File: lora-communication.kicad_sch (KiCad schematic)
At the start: 33 parts, among them J4 Conn_Coaxial, U401 SX1262, U402 PE4259, Y3 Crystal_GND24

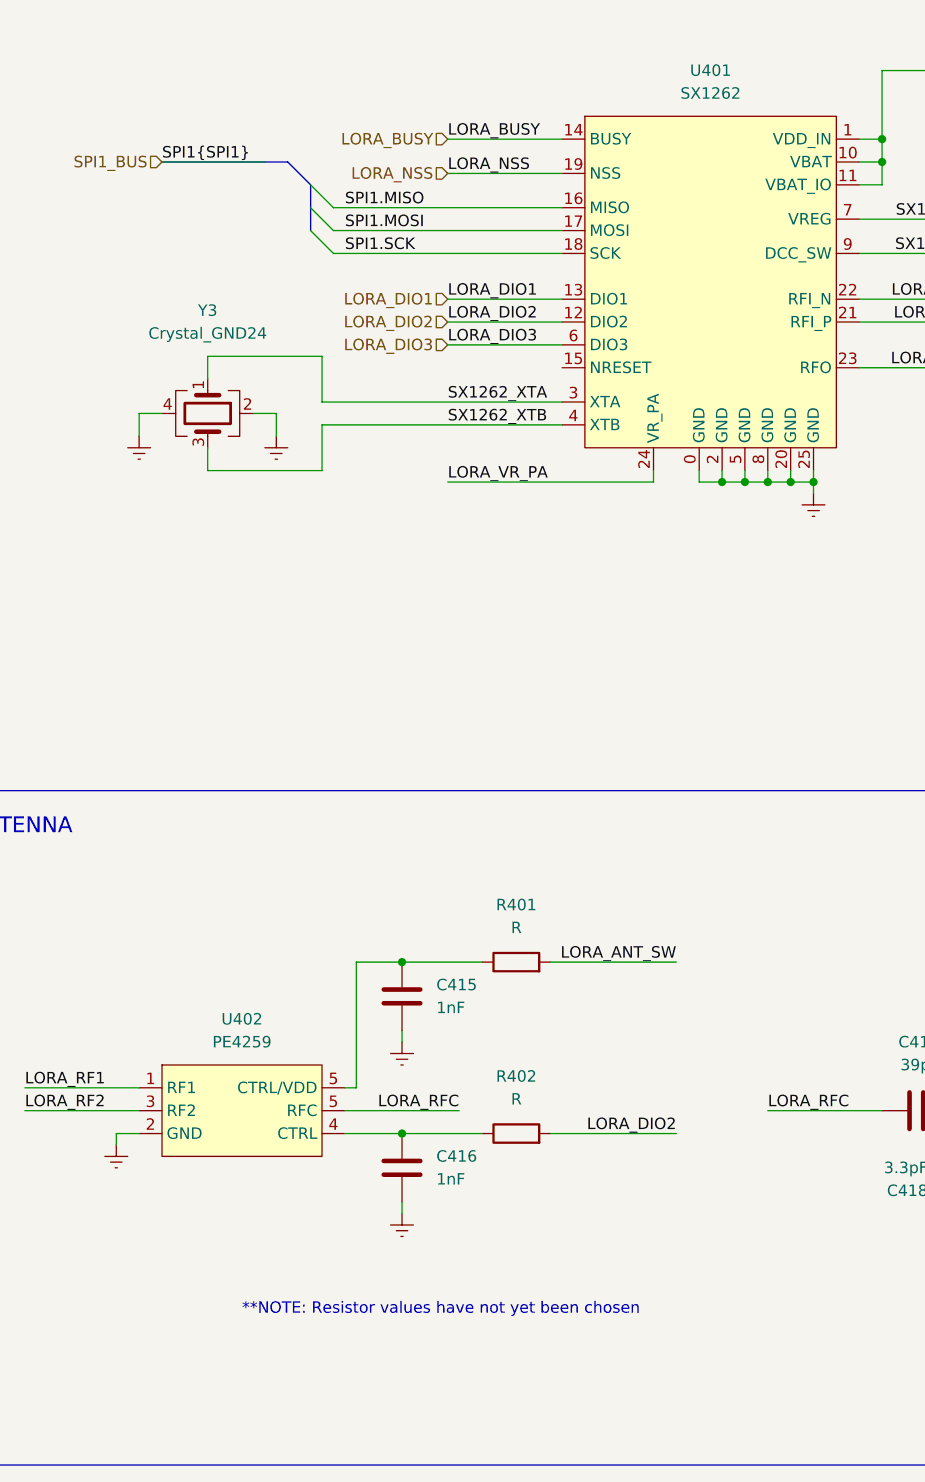
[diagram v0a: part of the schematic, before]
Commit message: updated bus aliases; added resistor values to RF section; added component to Fruitly_RF library
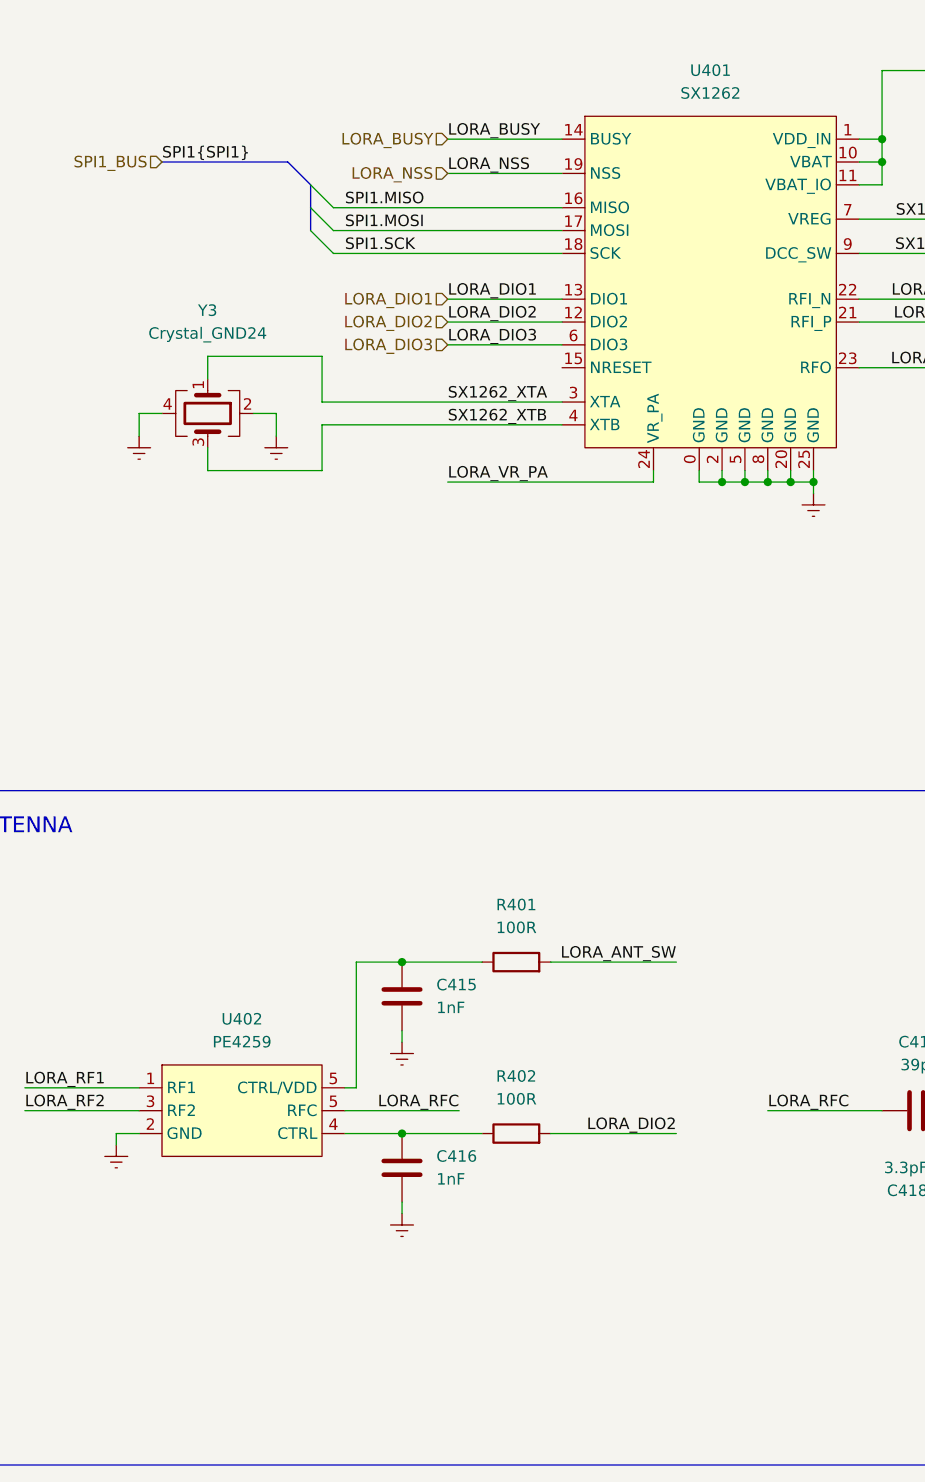
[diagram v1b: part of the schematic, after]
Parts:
- R401, R402: value R -> 100R
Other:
- note removed: "**NOTE: Resistor values have not yet been chosen"
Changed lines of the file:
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@@
     (company "Cerebral Systems Inc.")
   )
+  (bus_alias "SPI1" (members "MISO" "MOSI" "SCK"))
   (junction (at 110.49 87.63) (diameter 0) (color 0 0 0 0)
   )
@@
   )
   (wire (pts (xy 22.86 157.48) (xy 35.56 157.48))
-    (stroke (width 0) (type default) (color 0 0 0 0))
-  )
-  (wire (pts (xy 38.1 52.07) (xy 49.53 52.07))
     (stroke (width 0) (type default) (color 0 0 0 0))
   )
@@
   (text "ANTENNA IMPEDANCE MATCHING CIRCUIT" (at 177.8 81.28 0)
     (effects (font (size 1.75 1.75)) (justify left bottom))
-  )
-  (text "**NOTE: Resistor values have not yet been chosen" (at 46.99 180.34 0)
-    (effects (font (size 1.27 1.27)) (justify left bottom))
   )
   (label "SPI1.MISO" (at 58.42 57.15 0)
@@
     (in_bom yes) (on_board yes)
     (property "Reference" "R401" (id 0) (at 77.47 134.62 90))
-    (property "Value" "R" (id 1) (at 77.47 137.16 90))
+    (property "Value" "100R" (id 1) (at 77.47 137.16 90))
     (property "Footprint" "Resistor_SMD:R_0402_1005Metric" (id 2) (at 77.47 142.748 90)
       (effects (font (size 1.27 1.27)) hide)
@@
     (in_bom yes) (on_board yes)
     (property "Reference" "R402" (id 0) (at 77.47 153.67 90))
-    (property "Value" "R" (id 1) (at 77.47 156.21 90))
+    (property "Value" "100R" (id 1) (at 77.47 156.21 90))
     (property "Footprint" "Resistor_SMD:R_0402_1005Metric" (id 2) (at 77.47 161.798 90)
       (effects (font (size 1.27 1.27)) hide)

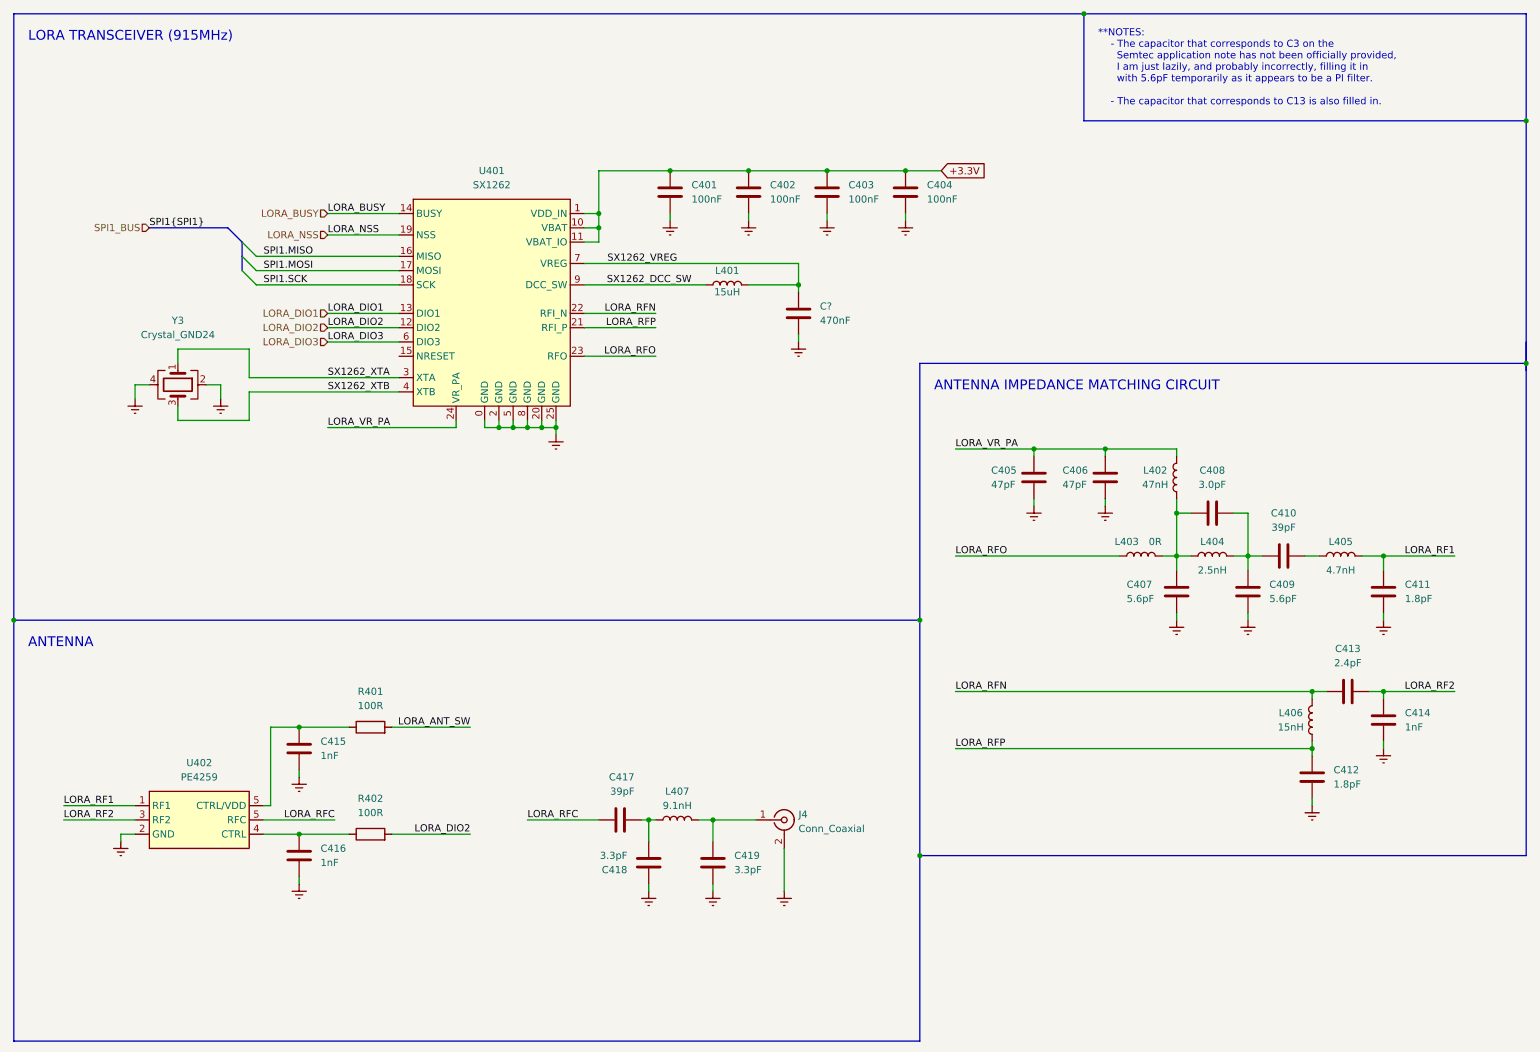
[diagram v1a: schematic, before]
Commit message: changed impedance matching circuit to IPD (integrated impedance device); updated RF switch
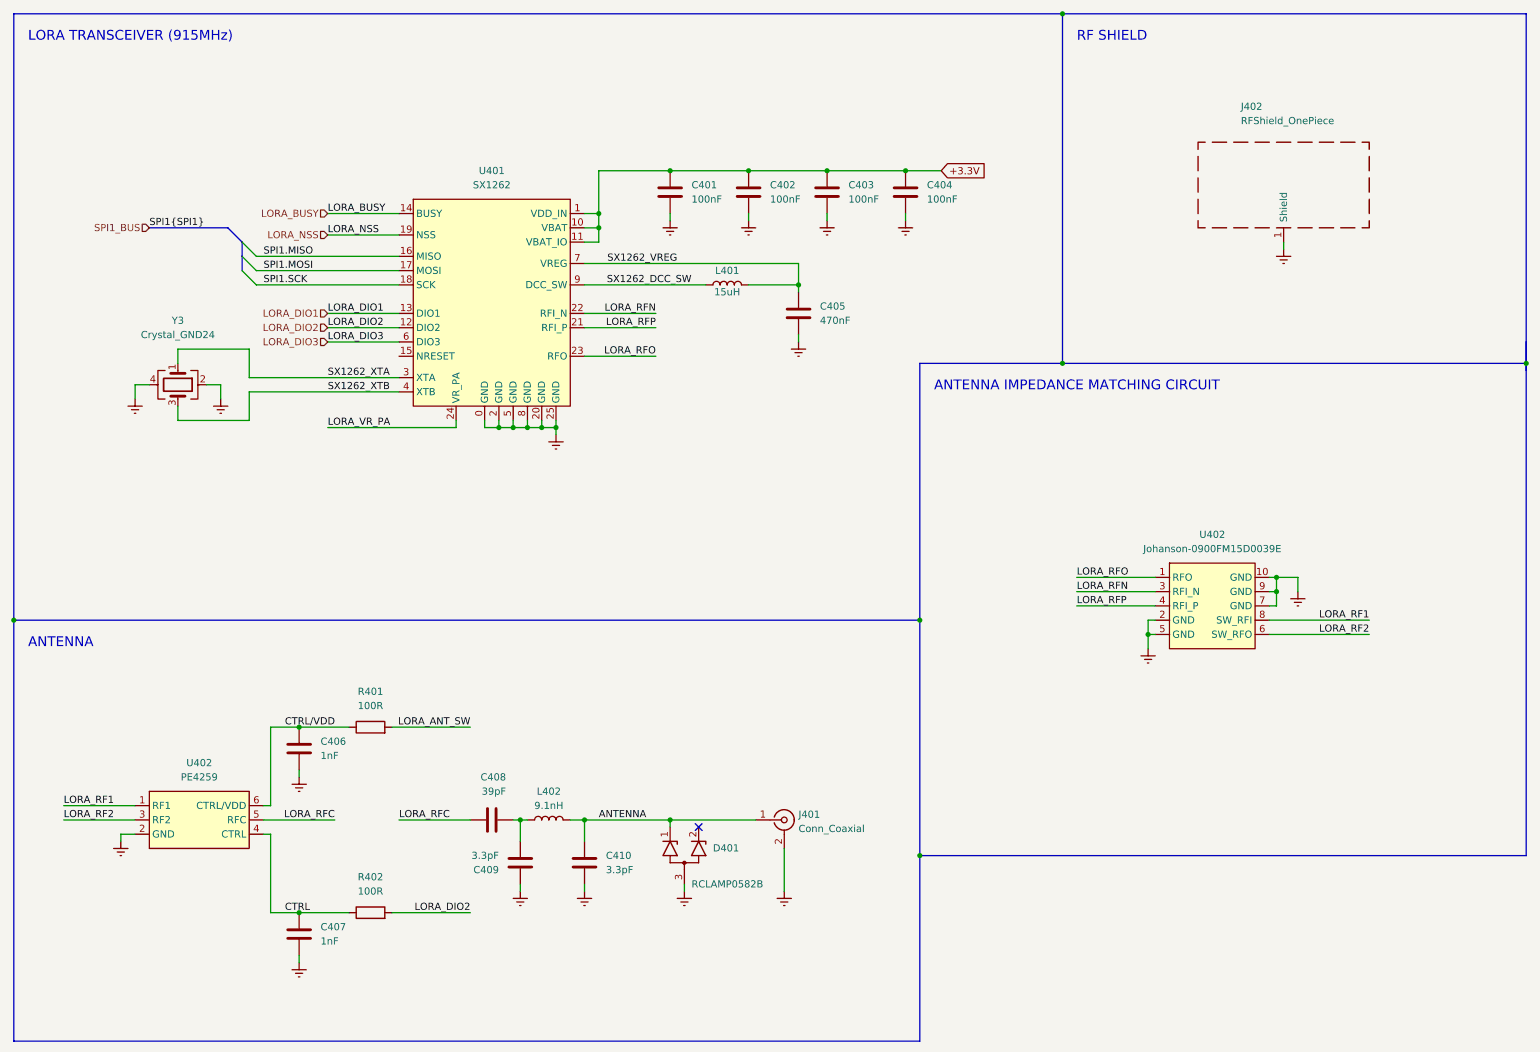
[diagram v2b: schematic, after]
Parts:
- removed C405, C406: 47pF, Capacitor_SMD:C_0402_1005Metric, symbol Device:C
- removed C407, C409: 5.6pF, Capacitor_SMD:C_0402_1005Metric, symbol Device:C
- removed C408: 3.0pF, Capacitor_SMD:C_0402_1005Metric, symbol Device:C
- removed C410: 39pF, Capacitor_SMD:C_0402_1005Metric, symbol Device:C
- removed C411, C412: 1.8pF, Capacitor_SMD:C_0402_1005Metric, symbol Device:C
- removed C413: 2.4pF, Capacitor_SMD:C_0402_1005Metric, symbol Device:C
- removed C414: 1nF, Capacitor_SMD:C_0402_1005Metric, symbol Device:C
- removed L402: 47nH, Inductor_SMD:L_0402_1005Metric, symbol Device:L
- removed L403: 0R, Inductor_SMD:L_0402_1005Metric, symbol Device:L
- removed L404: 2.5nH, Inductor_SMD:L_0402_1005Metric, symbol Device:L
- removed L405: 4.7nH, Inductor_SMD:L_0402_1005Metric, symbol Device:L
- removed L406: 15nH, Inductor_SMD:L_0402_1005Metric, symbol Device:L
- removed U402: PE4259, symbol Fruitfly_RF:PE4259
- added D401: RCLAMP0582B, Package_TO_SOT_SMD:SOT-416, symbol Power_Protection:RCLAMP0582B
- added J402: RFShield_OnePiece, RF_Shielding:Wuerth_36103205_20x20mm, symbol Device:RFShield_OnePiece
- added U402: PE4259, 6-lead_SC-70:6-lead_SC-70, symbol RF_Components:PE4259
- added U402: Johanson-0900FM15D0039E, 0900FM15D0039:0900FM15D0039, symbol RF_Components:Johanson-0900FM15D0039E
- gave numbers to parts that had none: 1
- renumbered C415 to C406, C416 to C407, C417 to C408, C418 to C409, C419 to C410, J4 to J401, L407 to L402
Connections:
- net Earth: now also D401.3 (A), J402.1 (Shield), U402.10 (GND), U402.2 (GND), U402.2 (GND), U402.5 (GND), U402.7 (GND), U402.9 (GND)
- net LORA_RF1: now also U402.1 (RF1), U402.8 (SW_RFI)
- net LORA_RF2: now also U402.3 (RF2), U402.6 (SW_RFO)
- net LORA_RFC: now also U402.5 (RFC)
- net LORA_RFN: now also U402.3 (RFI_N)
- net LORA_RFO: now also U402.1 (RFO)
- net LORA_RFP: now also U402.4 (RFI_P)
- net CTRL/VDD: now reaches C406.1, R401.1
- net CTRL/VDD: now also U402.6 (CTRL/VDD)
- net ANTENNA: now reaches C410.1, J401.1 (In), L402.2
- net ANTENNA: now also D401.1 (K1)
- net CTRL: now reaches C407.1, R402.1
- net CTRL: now also U402.4 (CTRL)
- no-connect marks 0 -> 1
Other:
- note added: "RF SHIELD"
- note removed: "**NOTES: - The capacitor that corresponds to C3 on the Semtec application note has not been officially provided, I am just lazily, and probably incorrectly, filling it in with 5.6pF temporarily as it appears to be a PI filter. - The capacitor that corresponds to C13 is also filled in."
- moved on the sheet: C407, C408, C409, C410, L402, R402

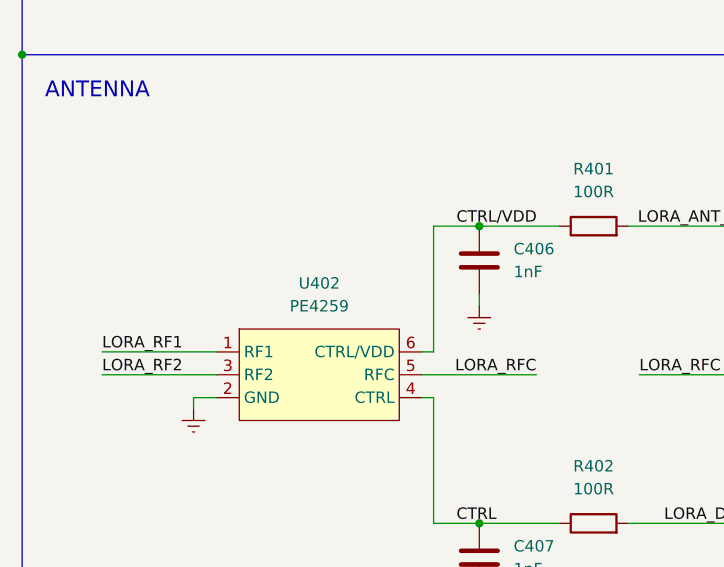
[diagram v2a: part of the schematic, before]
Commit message: updated ic reference designators
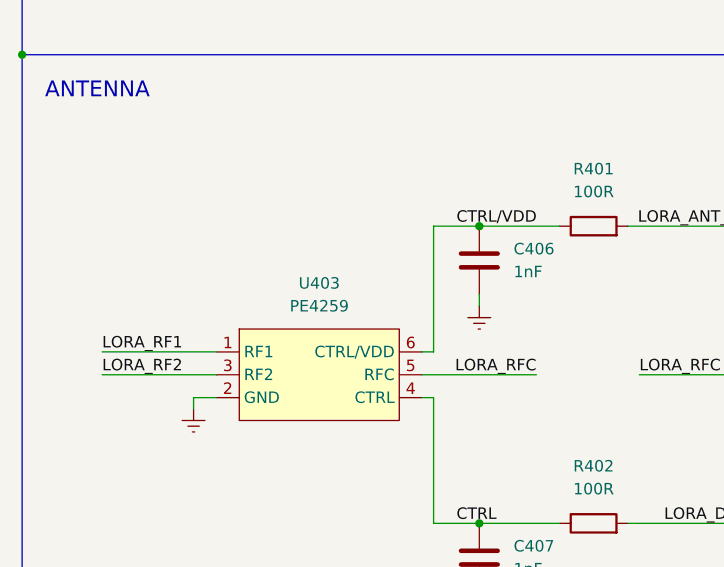
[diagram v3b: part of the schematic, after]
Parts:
- renumbered U402 to U403
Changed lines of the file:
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@@
   (symbol (lib_id "RF_Components:PE4259") (at 46.99 152.4 0) (unit 1)
     (in_bom yes) (on_board yes) (fields_autoplaced)
-    (property "Reference" "U402" (id 0) (at 46.99 147.32 0))
+    (property "Reference" "U403" (id 0) (at 46.99 147.32 0))
     (property "Value" "PE4259" (id 1) (at 46.99 149.86 0))
     (property "Footprint" "6-lead_SC-70:6-lead_SC-70" (id 2) (at 46.99 147.32 0)
